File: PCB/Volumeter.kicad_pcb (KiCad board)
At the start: 2 copper layers, 50.8 x 15.2 mm, 12 parts, among them SW1 SW_Push, U1 ATtiny85-20PU

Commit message: renamed project to volumeter
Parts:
- C1: footprint Capacitor_THT:CP_Radial_D4.0mm_P2.00mm -> Capacitor_THT:CP_Radial_D5.0mm_P2.50mm
- moved C1 0.63 mm to (28.6, 29.2)

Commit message: remove hole label
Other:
- board text added: "3.2mm"
- board text removed: "3mm"
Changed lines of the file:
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@@
     (clearance 1)
     (attr virtual)
-    (fp_text reference H1 (at 0 -3.75) (layer F.SilkS)
+    (fp_text reference H1 (at 0 -3.75) (layer F.SilkS) hide
       (effects (font (size 1 1) (thickness 0.15)))
     )
@@
     (effects (font (size 1 1) (thickness 0.15)))
   )
-  (gr_text 3mm (at 36.83 34.29) (layer F.SilkS)
+  (gr_text 3.2mm (at 38.735 28.575) (layer F.SilkS)
     (effects (font (size 1 1) (thickness 0.15)))
   )

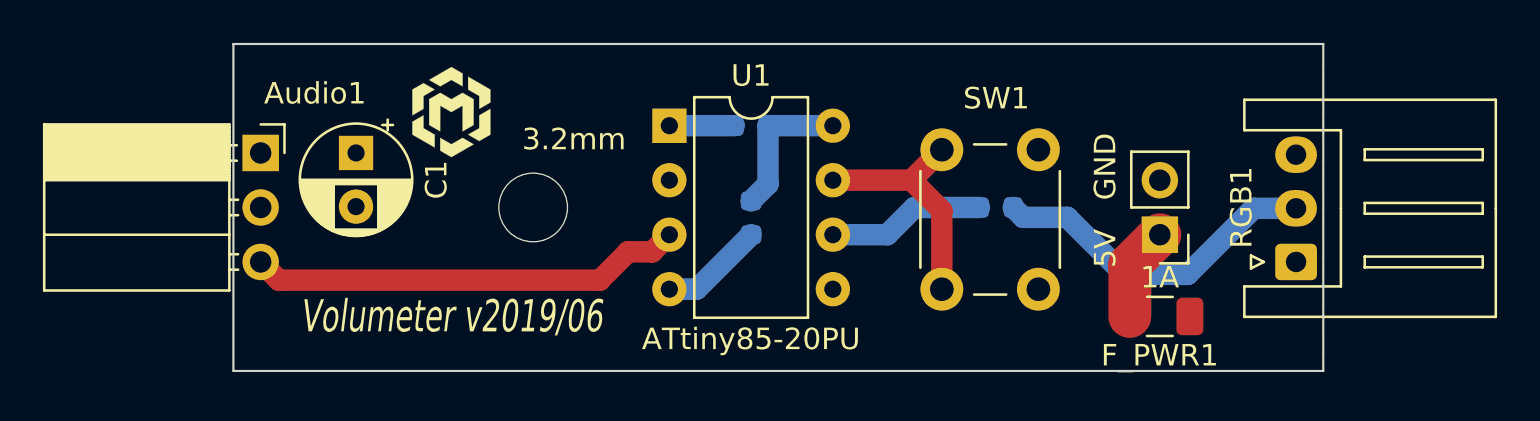
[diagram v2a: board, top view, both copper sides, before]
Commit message: use horizontal capacitor model
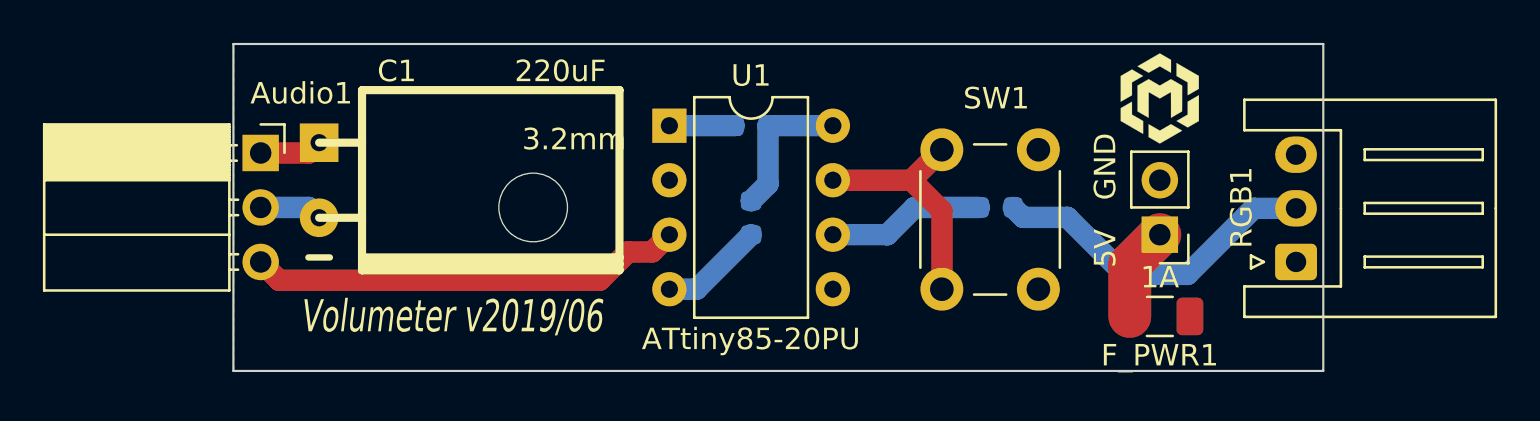
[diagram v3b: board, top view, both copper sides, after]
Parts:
- C1: value 100uF -> 220uF; footprint Capacitor_THT:CP_Radial_D5.0mm_P2.50mm -> w_capacitors:CP_8x11.5mm_hor
- moved G*** 33.0 mm to (66.0, 26.7)
- moved C1 1.27 mm to (28.6, 30.5), turned to 180 degrees
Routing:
- net +5V: track 6.85 -> 9.78 mm
- net GND: track 4.86 -> 7.79 mm
